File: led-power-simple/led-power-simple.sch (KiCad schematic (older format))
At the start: 38 parts, among them J1 Screw_Terminal_01x02, J2 Screw_Terminal_01x02, J3 Screw_Terminal_01x02, J4 Screw_Terminal_01x02, J5 Screw_Terminal_01x02, J6 Screw_Terminal_01x02, J7 Screw_Terminal_01x02, J8 Screw_Terminal_01x02, J9 Screw_Terminal_01x02, U1 LM7809_TO220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

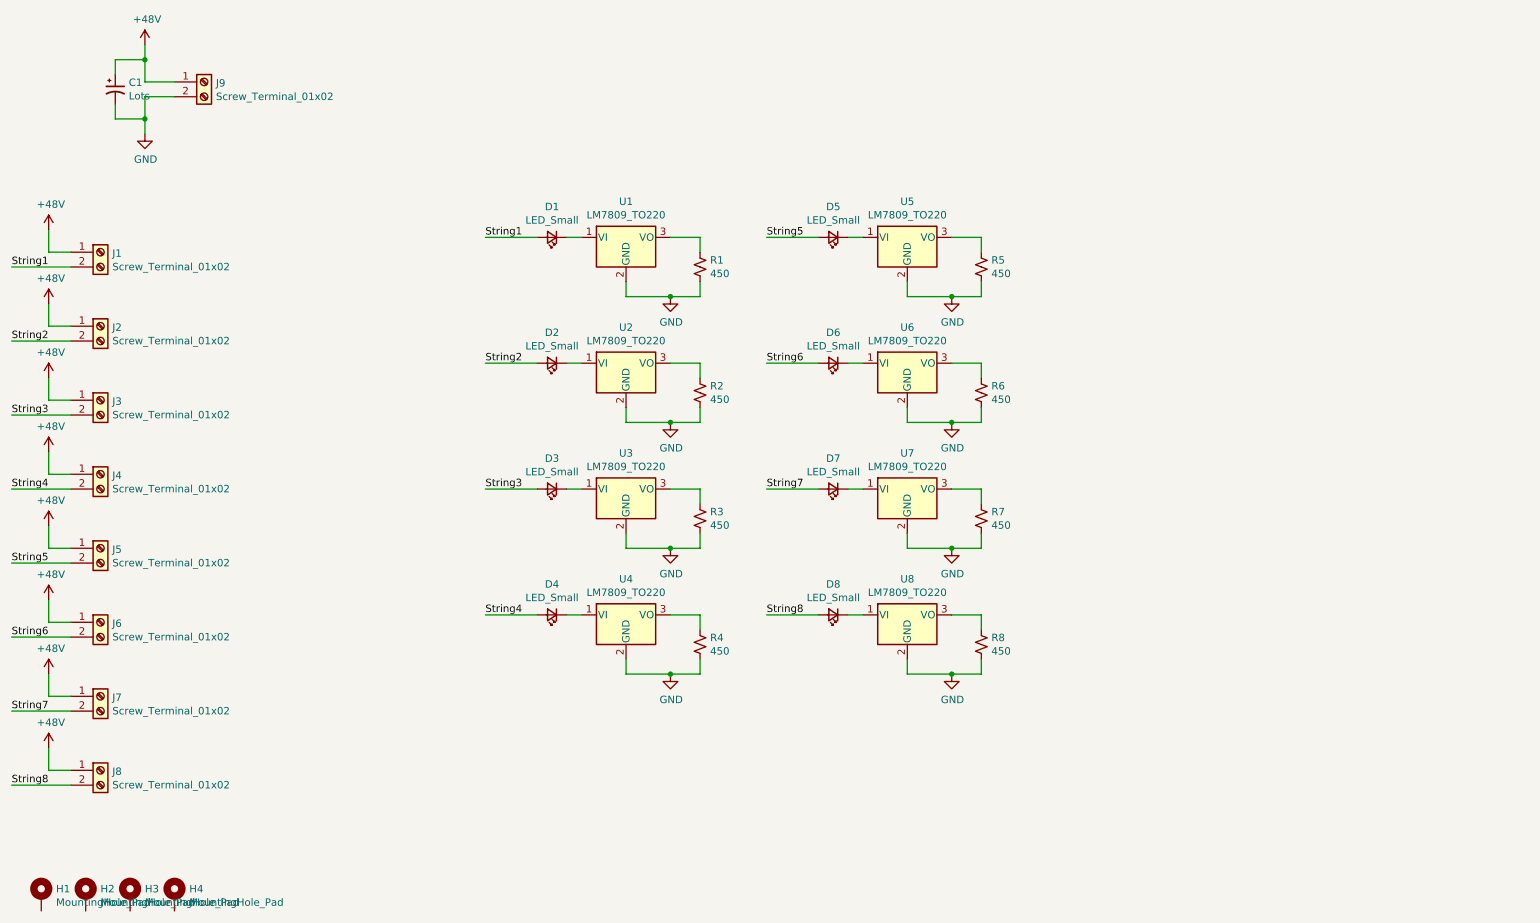
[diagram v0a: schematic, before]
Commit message: protective mosfet on power input. all THT parts
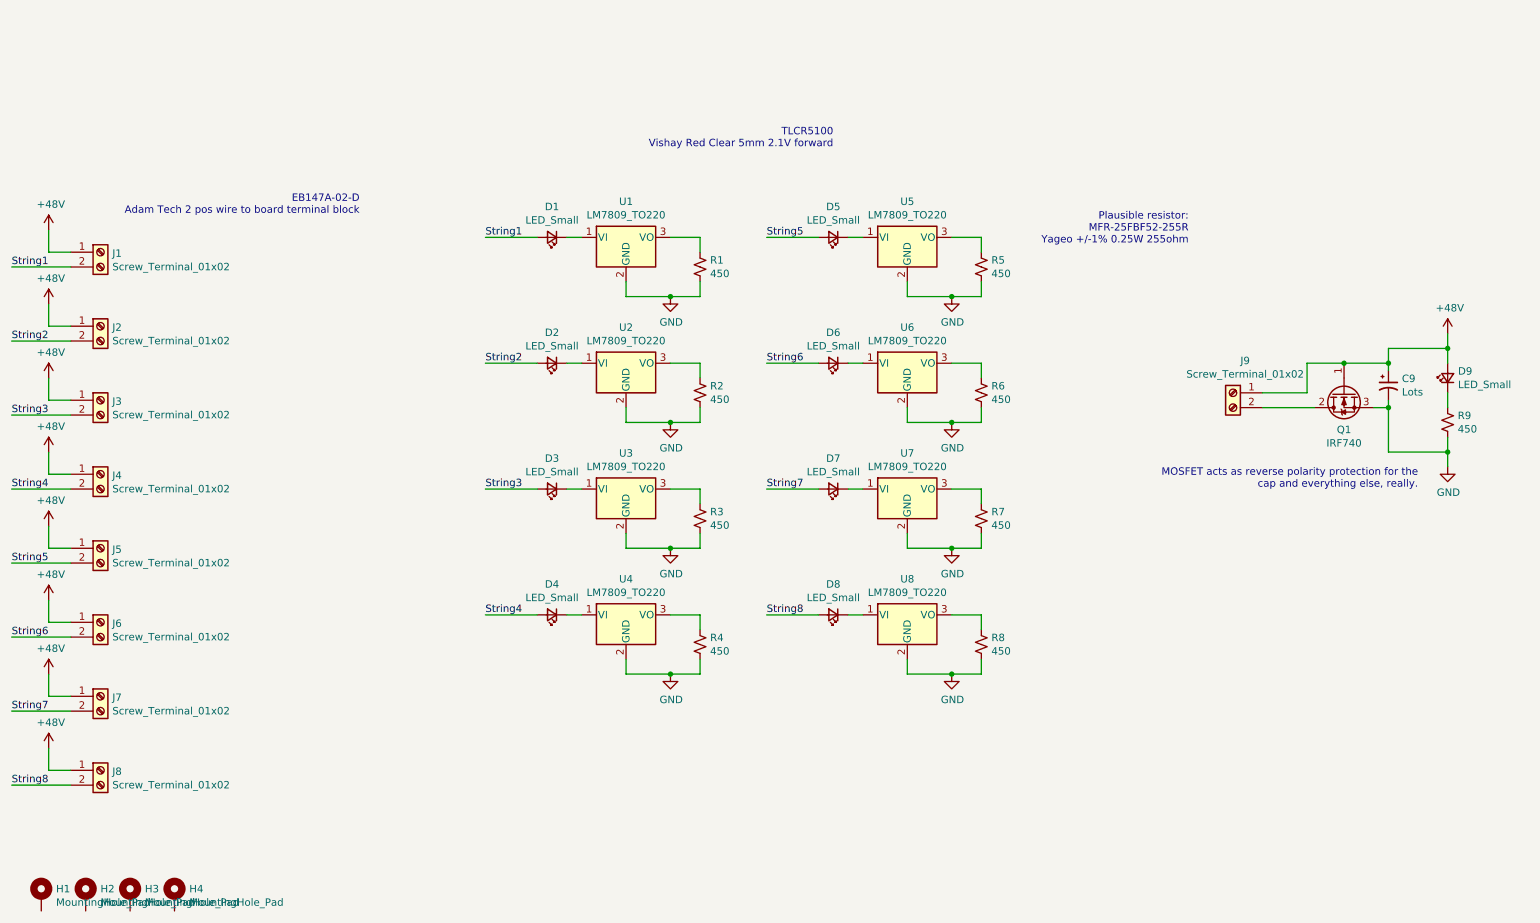
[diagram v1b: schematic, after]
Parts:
- added D9: LED_Small, LEDs:LED_D5.0mm, symbol Device:LED_Small
- added Q1: IRF740, TO_SOT_Packages_THT:TO-220-3_Vertical, symbol Transistor_FET:IRF740
- added R9: 450, Resistors_THT:R_Axial_DIN0207_L6.3mm_D2.5mm_P5.08mm_Vertical, symbol Device:R_Small_US
- D1, D2, D3, D4, D5, D6, D7, D8: footprint LEDs:LED_1206_HandSoldering -> LEDs:LED_D5.0mm
- renumbered C1 to C9
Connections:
- net +48V: now also D9.2 (A), Q1.1 (G)
- net GND: now also Q1.3 (S), R9.2; no longer J9.2 (Pin_2)
- new net: J9.2 (Pin_2), Q1.2 (D)
- new net: D9.1 (K), R9.1
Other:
- note added: "EB147A-02-D\nAdam Tech 2 pos wire to board terminal block"
- note added: "MOSFET acts as reverse polarity protection for the\ncap and everything else, really."
- note added: "Plausible resistor:\nMFR-25FBF52-255R\nYageo +/-1% 0.25W 255ohm"
- note added: "TLCR5100\nVishay Red Clear 5mm 2.1V forward"
- moved on the sheet: C9, J9
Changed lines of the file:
@@
 L Connector:Screw_Terminal_01x02 J9
 U 1 1 5FA6E729
-P 1850 1150
-F 0 "J9" H 1930 1142 50  0000 L CNN
-F 1 "Screw_Terminal_01x02" H 1930 1051 50  0000 L CNN
-F 2 "Connectors_Terminal_Blocks:TerminalBlock_bornier-2_P5.08mm" H 1850 1150 50  0001 C CNN
-F 3 "~" H 1850 1150 50  0001 C CNN
-	1    1850 1150
-	1    0    0    -1
-$EndComp
-Wire Wire Line
-	1650 1150 1450 1150
-Wire Wire Line
-	1450 1150 1450 1000
-Wire Wire Line
-	1650 1250 1450 1250
-Wire Wire Line
-	1450 1250 1450 1400
-$Comp
-L power:GND #PWR02
-U 1 1 5FA6F74C
-P 1450 1500
-F 0 "#PWR02" H 1450 1250 50  0001 C CNN
-F 1 "GND" H 1455 1327 50  0000 C CNN
-F 2 "" H 1450 1500 50  0001 C CNN
-F 3 "" H 1450 1500 50  0001 C CNN
-	1    1450 1500
-	1    0    0    -1
+P 8800 3250
+F 0 "J9" H 8718 3467 50  0000 C CNN
+F 1 "Screw_Terminal_01x02" H 8718 3376 50  0000 C CNN
+F 2 "Connectors_Terminal_Blocks:TerminalBlock_bornier-2_P5.08mm" H 8800 3250 50  0001 C CNN
+F 3 "~" H 8800 3250 50  0001 C CNN
+	1    8800 3250
+	-1   0    0    -1
 $EndComp
 $Comp
 L power:+48V #PWR01
 U 1 1 5FA6FB5A
-P 1450 900
-F 0 "#PWR01" H 1450 750 50  0001 C CNN
-F 1 "+48V" H 1465 1073 50  0000 C CNN
-F 2 "" H 1450 900 50  0001 C CNN
-F 3 "" H 1450 900 50  0001 C CNN
-	1    1450 900
+P 10250 2850
+F 0 "#PWR01" H 10250 2700 50  0001 C CNN
+F 1 "+48V" H 10265 3023 50  0000 C CNN
+F 2 "" H 10250 2850 50  0001 C CNN
+F 3 "" H 10250 2850 50  0001 C CNN
+	1    10250 2850
 	1    0    0    -1
 $EndComp
@@
 F 0 "D1" H 4200 1993 50  0000 C CNN
 F 1 "LED_Small" H 4200 2084 50  0000 C CNN
-F 2 "LEDs:LED_1206_HandSoldering" V 4200 2200 50  0001 C CNN
+F 2 "LEDs:LED_D5.0mm" V 4200 2200 50  0001 C CNN
 F 3 "~" V 4200 2200 50  0001 C CNN
 	1    4200 2200
@@
 F 0 "D2" H 4200 2843 50  0000 C CNN
 F 1 "LED_Small" H 4200 2934 50  0000 C CNN
-F 2 "LEDs:LED_1206_HandSoldering" V 4200 3050 50  0001 C CNN
+F 2 "LEDs:LED_D5.0mm" V 4200 3050 50  0001 C CNN
 F 3 "~" V 4200 3050 50  0001 C CNN
 	1    4200 3050
@@
 F 0 "D3" H 4200 3693 50  0000 C CNN
 F 1 "LED_Small" H 4200 3784 50  0000 C CNN
-F 2 "LEDs:LED_1206_HandSoldering" V 4200 3900 50  0001 C CNN
+F 2 "LEDs:LED_D5.0mm" V 4200 3900 50  0001 C CNN
 F 3 "~" V 4200 3900 50  0001 C CNN
 	1    4200 3900
@@
 F 0 "D4" H 4200 4543 50  0000 C CNN
 F 1 "LED_Small" H 4200 4634 50  0000 C CNN
-F 2 "LEDs:LED_1206_HandSoldering" V 4200 4750 50  0001 C CNN
+F 2 "LEDs:LED_D5.0mm" V 4200 4750 50  0001 C CNN
 F 3 "~" V 4200 4750 50  0001 C CNN
 	1    4200 4750
@@
 F 0 "D5" H 6100 1993 50  0000 C CNN
 F 1 "LED_Small" H 6100 2084 50  0000 C CNN
-F 2 "LEDs:LED_1206_HandSoldering" V 6100 2200 50  0001 C CNN
+F 2 "LEDs:LED_D5.0mm" V 6100 2200 50  0001 C CNN
 F 3 "~" V 6100 2200 50  0001 C CNN
 	1    6100 2200
@@
 F 0 "D6" H 6100 2843 50  0000 C CNN
 F 1 "LED_Small" H 6100 2934 50  0000 C CNN
-F 2 "LEDs:LED_1206_HandSoldering" V 6100 3050 50  0001 C CNN
+F 2 "LEDs:LED_D5.0mm" V 6100 3050 50  0001 C CNN
 F 3 "~" V 6100 3050 50  0001 C CNN
 	1    6100 3050
@@
 F 0 "D7" H 6100 3693 50  0000 C CNN
 F 1 "LED_Small" H 6100 3784 50  0000 C CNN
-F 2 "LEDs:LED_1206_HandSoldering" V 6100 3900 50  0001 C CNN
+F 2 "LEDs:LED_D5.0mm" V 6100 3900 50  0001 C CNN
 F 3 "~" V 6100 3900 50  0001 C CNN
 	1    6100 3900
@@
 F 0 "D8" H 6100 4543 50  0000 C CNN
 F 1 "LED_Small" H 6100 4634 50  0000 C CNN
-F 2 "LEDs:LED_1206_HandSoldering" V 6100 4750 50  0001 C CNN
+F 2 "LEDs:LED_D5.0mm" V 6100 4750 50  0001 C CNN
 F 3 "~" V 6100 4750 50  0001 C CNN
 	1    6100 4750
@@
 Connection ~ 6900 5150
 $Comp
-L Device:CP1_Small C1
+L Device:CP1_Small C9
 U 1 1 5FADE368
-P 1250 1200
-F 0 "C1" H 1341 1246 50  0000 L CNN
-F 1 "Lots" H 1341 1155 50  0000 L CNN
-F 2 "Capacitors_THT:CP_Radial_D16.0mm_P7.50mm" H 1250 1200 50  0001 C CNN
-F 3 "~" H 1250 1200 50  0001 C CNN
-	1    1250 1200
-	1    0    0    -1
-$EndComp
-Wire Wire Line
-	1250 1100 1250 1000
-Wire Wire Line
-	1250 1000 1450 1000
-Connection ~ 1450 1000
-Wire Wire Line
-	1450 1000 1450 900
-Wire Wire Line
-	1250 1300 1250 1400
-Wire Wire Line
-	1250 1400 1450 1400
-Connection ~ 1450 1400
-Wire Wire Line
-	1450 1400 1450 1500
+P 9850 3200
+F 0 "C9" H 9941 3246 50  0000 L CNN
+F 1 "Lots" H 9941 3155 50  0000 L CNN
+F 2 "Capacitors_THT:CP_Radial_D16.0mm_P7.50mm" H 9850 3200 50  0001 C CNN
+F 3 "~" H 9850 3200 50  0001 C CNN
+	1    9850 3200
+	1    0    0    -1
+$EndComp
+$Comp
+L Device:LED_Small D9
+U 1 1 5FB6BE15
+P 10250 3150
+F 0 "D9" V 10296 3080 50  0000 R CNN
+F 1 "LED_Small" V 10205 3080 50  0000 R CNN
+F 2 "LEDs:LED_D5.0mm" V 10250 3150 50  0001 C CNN
+F 3 "~" V 10250 3150 50  0001 C CNN
+	1    10250 3150
+	0    -1   -1   0
+$EndComp
+$Comp
+L Device:R_Small_US R9
+U 1 1 5FB6CFAB
+P 10250 3450
+F 0 "R9" H 10318 3496 50  0000 L CNN
+F 1 "450" H 10318 3405 50  0000 L CNN
+F 2 "Resistors_THT:R_Axial_DIN0207_L6.3mm_D2.5mm_P5.08mm_Vertical" H 10250 3450 50  0001 C CNN
+F 3 "~" H 10250 3450 50  0001 C CNN
+	1    10250 3450
+	1    0    0    -1
+$EndComp
+Text Notes 8500 2250 2    50   ~ 0
+Plausible resistor:\nMFR-25FBF52-255R\nYageo +/-1% 0.25W 255ohm
+$Comp
+L Transistor_FET:IRF740 Q1
+U 1 1 5FB76D8D
+P 9550 3250
+F 0 "Q1" V 9799 3250 50  0000 C CNN
+F 1 "IRF740" V 9890 3250 50  0000 C CNN
+F 2 "TO_SOT_Packages_THT:TO-220-3_Vertical" H 9800 3175 50  0001 L CIN
+F 3 "http://www.vishay.com/docs/91054/91054.pdf" H 9550 3250 50  0001 L CNN
+	1    9550 3250
+	0    -1   1    0
+$EndComp
+$Comp
+L power:GND #PWR0101
+U 1 1 5FBA3628
+P 10250 3750
+F 0 "#PWR0101" H 10250 3500 50  0001 C CNN
+F 1 "GND" H 10255 3577 50  0000 C CNN
+F 2 "" H 10250 3750 50  0001 C CNN
+F 3 "" H 10250 3750 50  0001 C CNN
+	1    10250 3750
+	1    0    0    -1
+$EndComp
+Wire Wire Line
+	9350 3350 9000 3350
+Wire Wire Line
+	9750 3350 9850 3350
+Wire Wire Line
+	9000 3250 9300 3250
+Wire Wire Line
+	9300 3250 9300 3050
+Wire Wire Line
+	9300 3050 9550 3050
+Wire Wire Line
+	9550 3050 9850 3050
+Connection ~ 9550 3050
+Wire Wire Line
+	9850 3100 9850 3050
+Wire Wire Line
+	9850 3300 9850 3350
+Wire Wire Line
+	10250 2850 10250 2950
+Wire Wire Line
+	10250 3250 10250 3350
+Wire Wire Line
+	10250 3550 10250 3650
+Wire Wire Line
+	9850 3350 9850 3650
+Wire Wire Line
+	9850 3650 10250 3650
+Connection ~ 9850 3350
+Connection ~ 10250 3650
+Wire Wire Line
+	10250 3650 10250 3750
+Wire Wire Line
+	9850 3050 9850 2950
+Wire Wire Line
+	9850 2950 10250 2950
+Connection ~ 9850 3050
+Connection ~ 10250 2950
+Wire Wire Line
+	10250 2950 10250 3050
+Text Notes 10050 3900 2    50   ~ 0
+MOSFET acts as reverse polarity protection for the\ncap and everything else, really.
+Text Notes 2900 2050 2    50   ~ 0
+EB147A-02-D\nAdam Tech 2 pos wire to board terminal block
+Text Notes 6100 1600 2    50   ~ 0
+TLCR5100\nVishay Red Clear 5mm 2.1V forward
 $EndSCHEMATC
